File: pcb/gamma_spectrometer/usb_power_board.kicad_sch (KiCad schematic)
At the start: 32 parts, among them J101 DX07S024WJ3R400, U101 LP5907MFX-3.3, U102 AMS1117-3.3, U103 FT231XQ, U104 TPS60400DBV

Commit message: Complete BOM: MPN and footprints for all components
Session 5 (2026-05-23) - full BOM assignment finished.

Components assigned (KiCad Symbol Fields + Footprints):
- 81 capacitors / 17 unique MPN (Yageo, Murata, Vishay, Holy Stone)
- 79 resistors / 28 unique MPN (Yageo RC/RT/RL/AC series)
- 3 inductors (Bourns SRN3015 + SRU5028)
- 2 LEDs (Foryard + Wurth 0805)
- 1 PTC fuse (MF-MSMF050-2)
- 1 ferrite bead (Murata BLM18EG121SN1D, 0603 - fixed from docs 0402)
- All active ICs (STM32G474, MAX1847, AD8000, FT231XQ, etc.)

Key design decisions:
- Standard bypass: 100nF X7R 0603 (easier hand soldering vs 0402)
- LED package 0805 (instead of 0402)
- C115 consolidated with C206 on single MPN (GRM32ER71A476KE15L)
- HV chain (1812 1kV X7R, 18x): Holy Stone C1812X104K102T
- AD8000 Cfb: GRM1555C1H1R0WA01D 1pF +/-0.05pF NP0
- R415: 50R -> 49.9R E96 (50R unavailable in catalog)
- L101/L102: SRN3015 (footprint Neosid SMS-ME3015, geometry verified)
- L103: SRU5028 (footprint L_Bourns_SRU5016, XY identical)

Documentation contradictions fixed:
- C115 MPN: GRM32ER61A476KE20L -> GRM32ER71A476KE15L
- FT231XS (SSOP-16) -> FT231XQ (QFN-20) - actual chip choice
- Tantalum MPN: TAJA106K016RNJ -> TR3B106K010C0750 (Vishay Low ESR)
- Inductor refs in usb_power_board_schematic.md updated

Remaining for PCB order:
- D202/D203 footprint: change SOD-123W -> SOD-123 (Diotec standard)
- J_PMT401: custom B14-38 footprint (during PCB layout)

Files:
- bom_fp_work.md - authoritative BOM with status, MPN, footprints, URLs
- pcb/gamma_spectrometer.net - fresh netlist with all MPN fields
- docs/session_context.md - session 5 final state

Co-Authored-By: Claude Sonnet 4.6 <noreply@anthropic.com>
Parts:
- C101, C104, C105, C112, C113: footprint (none) -> Capacitor_Tantalum_SMD:CP_EIA-3528-21_Kemet-B_HandSolder; PN (none) -> TR3B106K010C0750; Ссылка на покупку  (none) -> https://www.electronshik.ru/item/VISHAY/TR3B106K010C0750
- C102, C107, C108, C109, C110, C111, C114, C116: value 100nF -> 0.1uF; footprint (none) -> Capacitor_SMD:C_0603_1608Metric_Pad1.08x0.95mm_HandSolder; PN (none) -> CC0603JRX7R9BB104; Ссылка на покупку  (none) -> https://www.electronshik.ru/item/YAG/CC0603JRX7R9BB104
- C103: footprint (none) -> Capacitor_SMD:C_0805_2012Metric_Pad1.18x1.45mm_HandSolder; PN (none) -> CC0805JKX7R9BB105; Ссылка на покупку  (none) -> https://www.electronshik.ru/item/YAG/CC0805JKX7R9BB105
- C106: footprint (none) -> Capacitor_SMD:C_0805_2012Metric_Pad1.18x1.45mm_HandSolder; PN (none) -> GRM21BR61C475KA88L; Ссылка на покупку  (none) -> https://www.electronshik.ru/item/MUR/GRM21BR61C475KA88L
- C115: footprint (none) -> Capacitor_SMD:C_1210_3225Metric_Pad1.33x2.70mm_HandSolder; PN (none) -> GRM32ER71A476KE15L; Ссылка на покупку  (none) -> https://www.electronshik.ru/item/MUR/GRM32ER71A476KE15L
- D101: footprint (none) -> LED_SMD:LED_0805_2012Metric_Pad1.15x1.40mm_HandSolder; PN (none) -> FYLS-0805UBC; Ссылка на покупку  (none) -> https://www.electronshik.ru/item/FORYARD/FYLS-0805UBC
- D102: footprint (none) -> LED_SMD:LED_0805_2012Metric_Pad1.15x1.40mm_HandSolder; PN (none) -> 150080GS75000; Ссылка на покупку  (none) -> https://www.electronshik.ru/item/WURTH/150080GS75000
- F101: footprint (none) -> Fuse:Fuse_1812_4532Metric_Pad1.30x3.40mm_HandSolder; PN (none) -> MF-MSMF050-2; Ссылка на покупку  (none) -> https://www.electronshik.ru/item/JEMETE/MF-MSMF050-2
- J101: PN (none) -> DX07S024WJ3R400
- L101, L102: footprint (none) -> Inductor_SMD:L_Neosid_SMS-ME3015; PN (none) -> SRN3015-470M; Ссылка на покупку  (none) -> https://www.electronshik.ru/item/BOURNS/SRN3015-470M
- L103: footprint (none) -> Inductor_SMD:L_Bourns_SRU5016_5.2x5.2mm; PN (none) -> SRU5028-101Y; Ссылка на покупку  (none) -> https://www.electronshik.ru/item/BOURNS/SRU5028-101Y
- R101, R102: footprint (none) -> Resistor_SMD:R_0603_1608Metric_Pad0.98x0.95mm_HandSolder; PN (none) -> RT0603BRD07330RL; Ссылка на покупку  (none) -> https://www.electronshik.ru/item/YAG/RT0603BRD07330RL
- R_CC101, R_CC102: footprint (none) -> Resistor_SMD:R_0603_1608Metric_Pad0.98x0.95mm_HandSolder; PN (none) -> RC0603FR-075K1L; Ссылка на покупку  (none) -> https://www.electronshik.ru/item/YAG/RC0603FR-075K1L
- U101: PN (none) -> LP5907MFX-3.3
- U102: PN (none) -> AMS1117-3.3
- U103: PN (none) -> FT231XQ
- U104: PN (none) -> TPS60400DBV
- U_ESD101: PN (none) -> PRTR5V0U2X

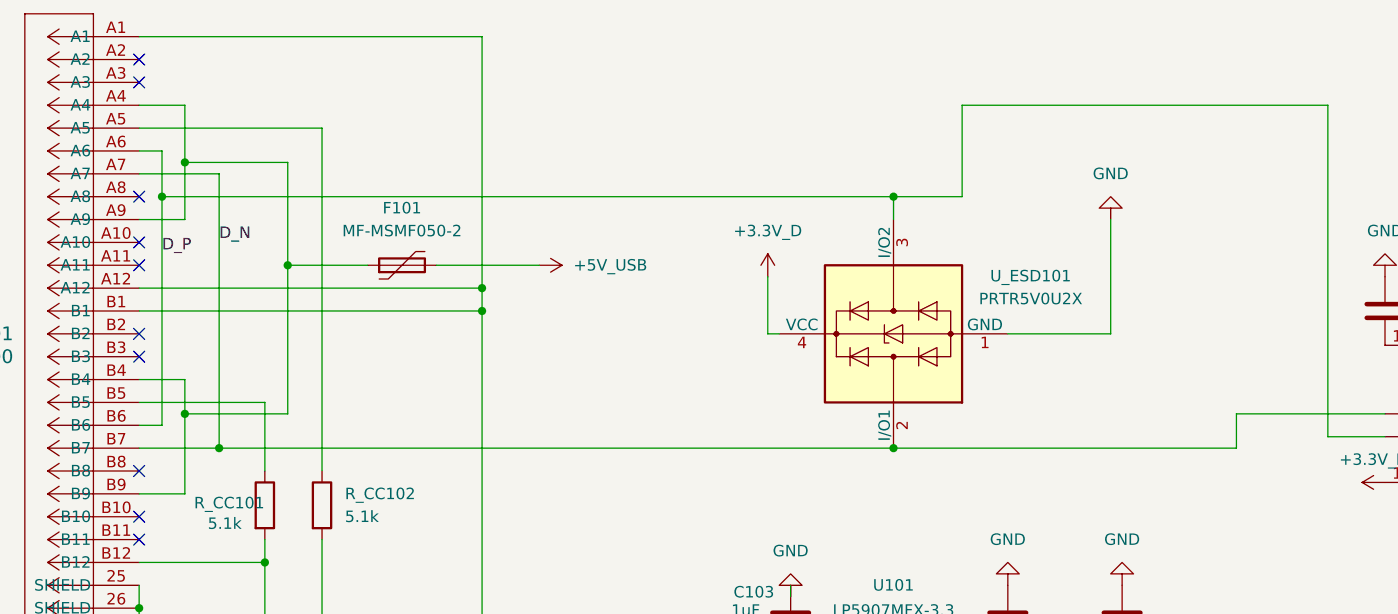
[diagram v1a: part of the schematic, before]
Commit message: pcb: расположение символов в схеме USB + дефолт пэда в проекте
- usb_power_board.kicad_sch: перестановка позиций символов/проводов
  (электрических изменений нет — связи, номиналы, метки прежние).
- .kicad_pro: дефолтный размер пэда -> сверло 1.5 / 2.5x2.5 (под цанг-пины).

Co-Authored-By: Claude Opus 4.8 <noreply@anthropic.com>
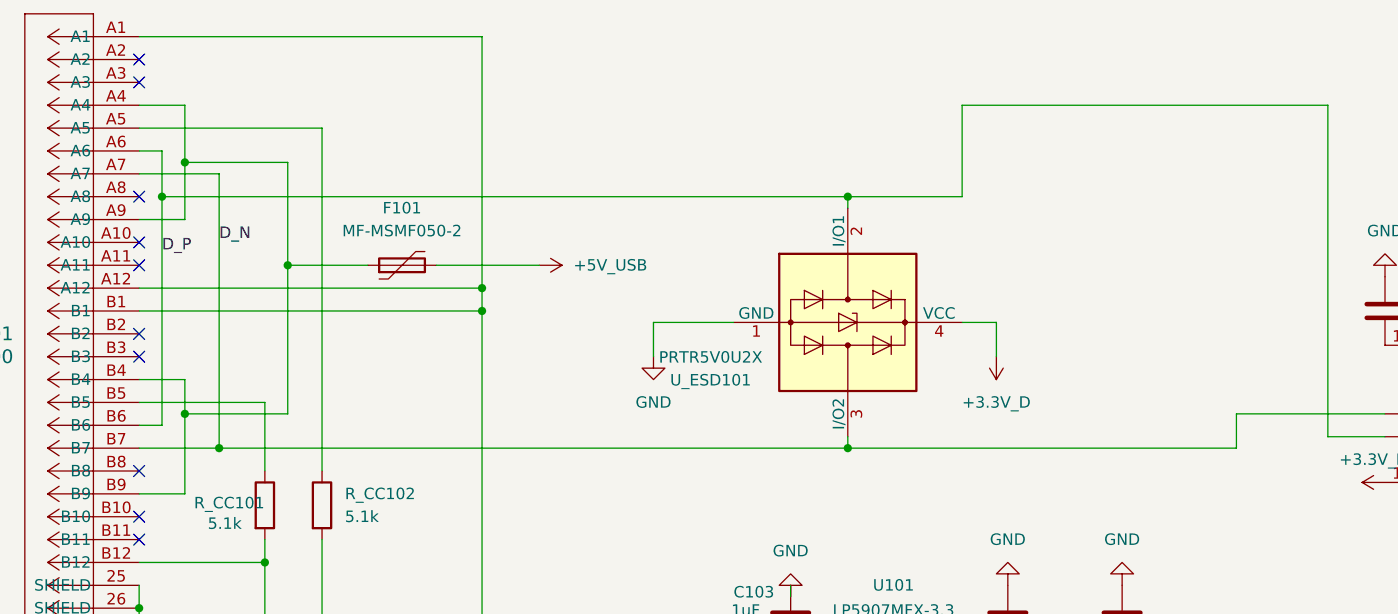
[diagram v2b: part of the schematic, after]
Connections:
- net D_N: now also U_ESD101.3 (I/O2); no longer U_ESD101.2 (I/O1)
- net D_P: now also U_ESD101.2 (I/O1); no longer U_ESD101.3 (I/O2)
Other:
- moved on the sheet: U_ESD101
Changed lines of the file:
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@@
 	)
 	(junction
+		(at 148.59 77.47)
+		(diameter 0)
+		(color 0 0 0 0)
+	)
+	(junction
+		(at 148.59 105.41)
+		(diameter 0)
+		(color 0 0 0 0)
+	)
+	(junction
 		(at 74.93 125.73)
 		(diameter 0)
@@
 	)
 	(junction
-		(at 153.67 105.41)
-		(diameter 0)
-		(color 0 0 0 0)
-	)
-	(junction
 		(at 83.82 160.02)
 		(diameter 0)
@@
 	)
 	(junction
-		(at 153.67 77.47)
-		(diameter 0)
-		(color 0 0 0 0)
-	)
-	(junction
 		(at 276.86 161.29)
 		(diameter 0)
@@
 	(wire
 		(pts
-			(xy 153.67 77.47) (xy 153.67 80.01)
+			(xy 148.59 105.41) (xy 191.77 105.41)
 		)
 		(stroke
@@
 	(wire
 		(pts
-			(xy 139.7 92.71) (xy 140.97 92.71)
+			(xy 165.1 91.44) (xy 161.29 91.44)
+		)
+		(stroke
+			(width 0)
+			(type default)
+		)
+	)
+	(wire
+		(pts
+			(xy 148.59 77.47) (xy 161.29 77.47)
 		)
 		(stroke
@@
 	(wire
 		(pts
-			(xy 153.67 105.41) (xy 191.77 105.41)
+			(xy 78.74 105.41) (xy 148.59 105.41)
 		)
 		(stroke
@@
 	(wire
 		(pts
-			(xy 166.37 92.71) (xy 177.8 92.71)
+			(xy 135.89 91.44) (xy 127 91.44)
 		)
 		(stroke
@@
 	(wire
 		(pts
-			(xy 139.7 86.36) (xy 139.7 92.71)
+			(xy 165.1 95.25) (xy 165.1 91.44)
 		)
 		(stroke
@@
 	(wire
 		(pts
-			(xy 78.74 105.41) (xy 153.67 105.41)
-		)
-		(stroke
-			(width 0)
-			(type default)
-		)
-	)
-	(wire
-		(pts
 			(xy 69.85 120.65) (xy 69.85 123.19)
 		)
@@
 	(wire
 		(pts
-			(xy 177.8 80.01) (xy 177.8 92.71)
+			(xy 127 95.25) (xy 127 91.44)
 		)
 		(stroke
@@
 	(wire
 		(pts
-			(xy 153.67 77.47) (xy 161.29 77.47)
+			(xy 78.74 105.41) (xy 69.85 105.41)
 		)
 		(stroke
@@
 	(wire
 		(pts
-			(xy 78.74 105.41) (xy 69.85 105.41)
+			(xy 107.95 90.17) (xy 107.95 125.73)
 		)
 		(stroke
@@
 	(wire
 		(pts
-			(xy 107.95 90.17) (xy 107.95 125.73)
+			(xy 69.85 72.39) (xy 72.39 72.39)
 		)
 		(stroke
@@
 	(wire
 		(pts
-			(xy 69.85 72.39) (xy 72.39 72.39)
+			(xy 260.35 161.29) (xy 264.16 161.29)
 		)
 		(stroke
@@
 	(wire
 		(pts
-			(xy 260.35 161.29) (xy 264.16 161.29)
+			(xy 69.85 123.19) (xy 69.85 125.73)
 		)
 		(stroke
@@
 	(wire
 		(pts
-			(xy 69.85 123.19) (xy 69.85 125.73)
+			(xy 90.17 115.57) (xy 90.17 125.73)
 		)
 		(stroke
@@
 	(wire
 		(pts
-			(xy 90.17 115.57) (xy 90.17 125.73)
+			(xy 72.39 77.47) (xy 148.59 77.47)
 		)
 		(stroke
@@
 	(wire
 		(pts
-			(xy 72.39 77.47) (xy 153.67 77.47)
+			(xy 148.59 104.14) (xy 148.59 105.41)
 		)
 		(stroke
@@
 	(wire
 		(pts
+			(xy 148.59 77.47) (xy 148.59 78.74)
+		)
+		(stroke
+			(width 0)
+			(type default)
+		)
+	)
+	(wire
+		(pts
 			(xy 215.9 161.29) (xy 218.44 161.29)
 		)
@@
 	(symbol
 		(lib_id "Power_Protection:PRTR5V0U2X")
-		(at 153.67 92.71 90)
+		(at 148.59 91.44 270)
 		(unit 1)
 		(exclude_from_sim no)
@@
 		(fields_autoplaced yes)
 		(property "Reference" "U_ESD101"
-			(at 168.91 86.2898 90)
+			(at 133.35 97.8602 90)
 			(effects
 				(font
@@
 		)
 		(property "Value" "PRTR5V0U2X"
-			(at 168.91 88.8298 90)
+			(at 133.35 95.3202 90)
 			(effects
 				(font
@@
 		)
 		(property "Footprint" "Package_TO_SOT_SMD:SOT-143"
-			(at 153.67 91.186 0)
+			(at 148.59 92.964 0)
 			(effects
 				(font
@@
 		)
 		(property "Datasheet" "https://assets.nexperia.com/documents/data-sheet/PRTR5V0U2X.pdf"
-			(at 153.67 91.186 0)
+			(at 148.59 92.964 0)
 			(effects
 				(font
@@
 		)
 		(property "Description" "Ultra low capacitance double rail-to-rail ESD protection diode, SOT-143"
-			(at 153.67 92.71 0)
+			(at 148.59 91.44 0)
 			(effects
 				(font
@@
 		)
 		(property "KLC_S3.3" ""
-			(at 153.67 92.71 90)
+			(at 148.59 91.44 90)
 			(effects
 				(font
@@
 		)
 		(property "KLC_S4.1" ""
-			(at 153.67 92.71 90)
+			(at 148.59 91.44 90)
 			(effects
 				(font
@@
 		)
 		(property "Ссылка на покупку " "https://www.electronshik.ru/item/YOUTAI/PRTR5V0U2X"
-			(at 153.67 92.71 90)
+			(at 148.59 91.44 90)
 			(effects
 				(font
@@
 		)
 		(property "PN" "PRTR5V0U2X"
-			(at 153.67 92.71 90)
+			(at 148.59 91.44 90)
 			(effects
 				(font
@@
 	(symbol
 		(lib_id "power:+3.3V")
-		(at 139.7 86.36 0)
+		(at 165.1 95.25 180)
 		(unit 1)
 		(exclude_from_sim no)
@@
 		(fields_autoplaced yes)
 		(property "Reference" "#+3.3V_D0101"
-			(at 139.7 90.17 0)
+			(at 165.1 91.44 0)
 			(effects
 				(font
@@
 		)
 		(property "Value" "+3.3V_D"
-			(at 139.7 81.28 0)
+			(at 165.1 100.33 0)
 			(effects
 				(font
@@
 		)
 		(property "Footprint" ""
-			(at 139.7 86.36 0)
+			(at 165.1 95.25 0)
 			(effects
 				(font
@@
 		)
 		(property "Datasheet" ""
-			(at 139.7 86.36 0)
+			(at 165.1 95.25 0)
 			(effects
 				(font
@@
 		)
 		(property "Description" "Power symbol creates a global label with name \"+3.3V\""
-			(at 139.7 86.36 0)
+			(at 165.1 95.25 0)
 			(effects
 				(font
@@
 	(symbol
 		(lib_id "power:GND")
-		(at 177.8 80.01 180)
+		(at 127 95.25 0)
 		(unit 1)
 		(exclude_from_sim no)
@@
 		(fields_autoplaced yes)
 		(property "Reference" "#PWR0111"
-			(at 177.8 73.66 0)
+			(at 127 101.6 0)
 			(effects
 				(font
@@
 		)
 		(property "Value" "GND"
-			(at 177.8 74.93 0)
+			(at 127 100.33 0)
 			(effects
 				(font
@@
 		)
 		(property "Footprint" ""
-			(at 177.8 80.01 0)
+			(at 127 95.25 0)
 			(effects
 				(font
@@
 		)
 		(property "Datasheet" ""
-			(at 177.8 80.01 0)
+			(at 127 95.25 0)
 			(effects
 				(font
@@
 		)
 		(property "Description" "Power symbol creates a global label with name \"GND\" , ground"
-			(at 177.8 80.01 0)
+			(at 127 95.25 0)
 			(effects
 				(font

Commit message: pcb: земля МК подключена, C320 удалён, C314/C317 → 1 мкФ, SWD-пятаки убраны
Плата МК:
- все GND-выводы U302 подключены (15, 27/VSSA, 40, 50 висели);
  зона GND на F.Cu: зазор 0.5 → 0.25 мм, зазор термобарьера → 0.2 мм;
  GND-виа 41 → 97. Остаётся: выводы 50 и 61 на одной спице (starved_thermal).
- TP_SWD301 удалён: прошивка — проводами к выводам 63/64/7 U302.

Схема МК (ревью REVIEW_critic_2026-09-15, находки 1.1 и 1.3, вариант V2):
- C320 удалён (100 нФ на PB0 делил сигнал ×0.5 вместе с C314);
- C314, C317: 100 нФ → 1 мкФ (CC0603JRX7R7BB105), τ связей ~1 мс.

USB-плата: J101 на проектной копии футпринта USB-C (экран на GND).

Co-Authored-By: Claude Opus 5 (1M context) <noreply@anthropic.com>
Claude-Session: https://claude.ai/code/session_018uEKxzknn1WsQbGcTkkQF5
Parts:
- J101: footprint Connector_USB:USB_C_Receptacle_JAE_DX07S024WJ3R400 -> посадочные места:USB_C_Receptacle_JAE_DX07S024WJ3R400
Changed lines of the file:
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@@
 			)
 		)
-		(property "Footprint" "Connector_USB:USB_C_Receptacle_JAE_DX07S024WJ3R400"
+		(property "Footprint" "посадочные места:USB_C_Receptacle_JAE_DX07S024WJ3R400"
 			(at 69.85 59.69 0)
 			(effects
